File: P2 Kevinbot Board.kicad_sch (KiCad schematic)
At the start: 40 parts, among them J1 Screw_Terminal_01x02, J10 Conn_01x04, J11 Conn_01x04_Male, J12 Conn_02x06_Odd_Even, J13 Conn_01x04, J14 Conn_01x02, J15 Conn_01x04, J16 Conn_02x06_Odd_Even, J2 Conn_01x03_Male, J3 Screw_Terminal_01x02, J30 Conn_01x02_Pin, J31 Conn_01x02, J4 Screw_Terminal_01x02, J5 Screw_Terminal_01x02, J6 Conn_02x06_Odd_Even, J7 Conn_01x04, J8 Conn_02x06_Odd_Even, J9 Screw_Terminal_01x02, Q1 IRLML6402, SW1 SW_Push, U1 P2_EDGE_MODULE_SOCKET, U2 DS18B20

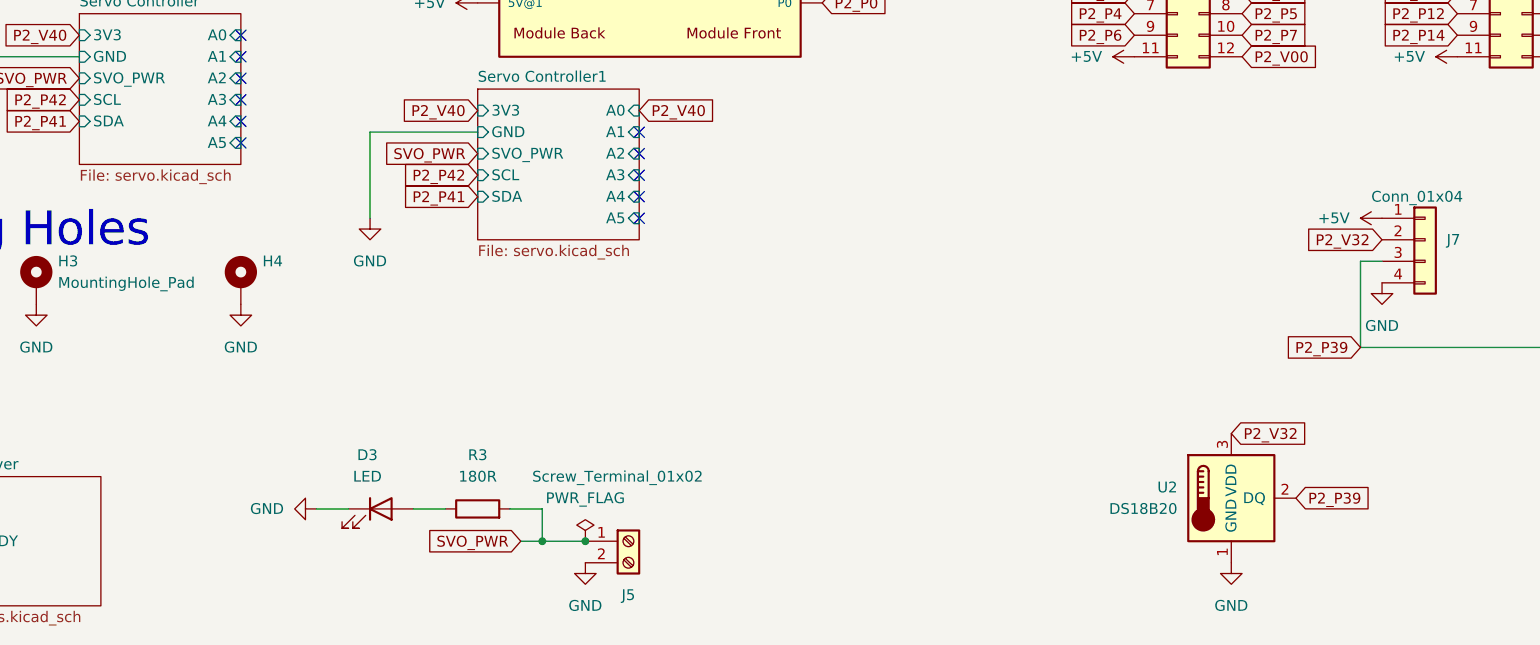
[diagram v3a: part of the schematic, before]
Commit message: Add servo fuse, increase trace width
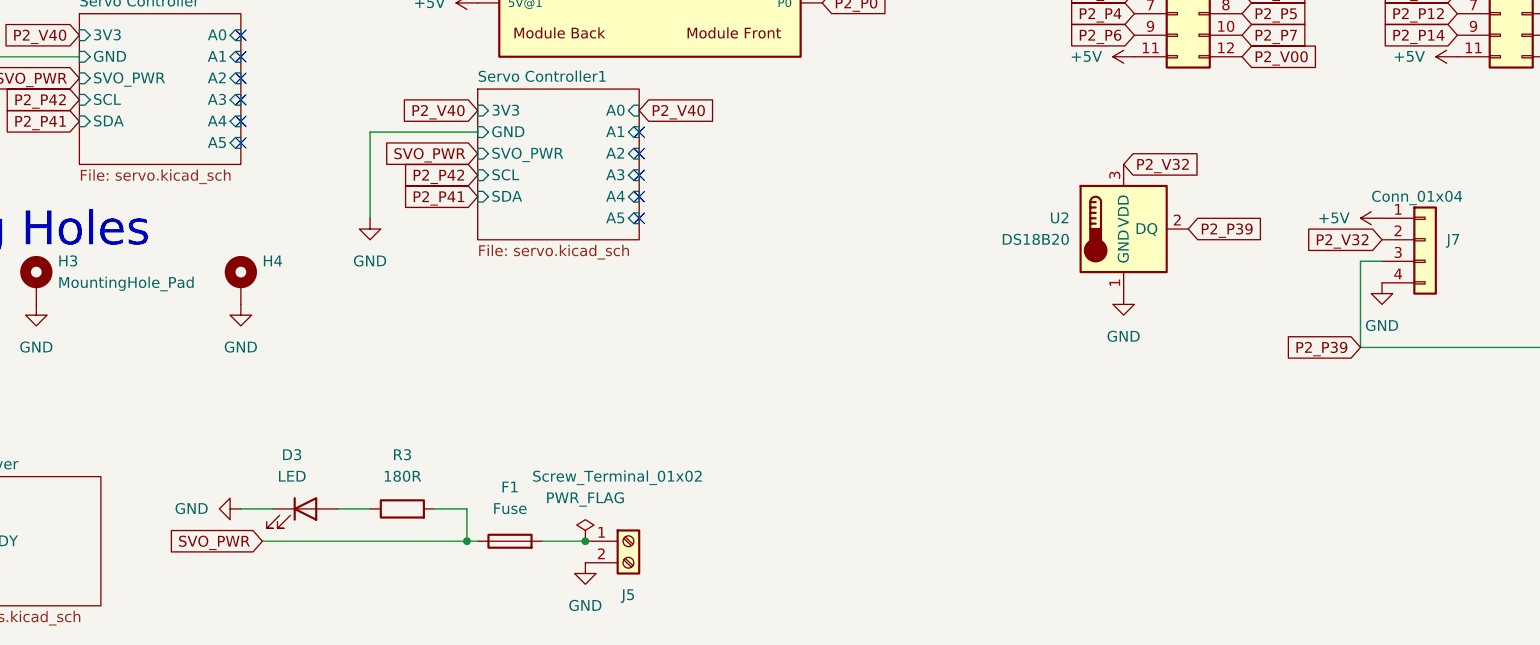
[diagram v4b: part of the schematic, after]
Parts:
- added F1: Fuse, symbol Device:Fuse
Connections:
- net SVO_PWR: now also F1.1; no longer J5.1 (Pin_1)
- new net: F1.2, J5.1 (Pin_1)
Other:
- moved on the sheet: D3, R3, U2
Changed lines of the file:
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@@
 	)
 	(junction
-		(at 133.35 189.23)
+		(at 284.48 69.85)
 		(diameter 0)
 		(color 0 0 0 0)
 	)
 	(junction
-		(at 284.48 69.85)
+		(at 304.8 166.37)
 		(diameter 0)
 		(color 0 0 0 0)
 	)
 	(junction
-		(at 304.8 166.37)
+		(at 198.12 87.63)
 		(diameter 0)
 		(color 0 0 0 0)
 	)
 	(junction
-		(at 138.43 189.23)
+		(at 39.37 33.02)
 		(diameter 0)
 		(color 0 0 0 0)
 	)
 	(junction
-		(at 198.12 87.63)
+		(at 138.43 189.23)
 		(diameter 0)
 		(color 0 0 0 0)
 	)
 	(junction
-		(at 39.37 33.02)
+		(at 273.05 69.85)
 		(diameter 0)
 		(color 0 0 0 0)
 	)
 	(junction
-		(at 273.05 69.85)
+		(at 124.46 189.23)
 		(diameter 0)
 		(color 0 0 0 0)
@@
 	(wire
 		(pts
-			(xy 118.11 185.42) (xy 121.92 185.42)
+			(xy 133.35 189.23) (xy 138.43 189.23)
 		)
 		(stroke
@@
 	(wire
 		(pts
-			(xy 303.53 74.93) (xy 300.99 74.93)
+			(xy 109.22 185.42) (xy 113.03 185.42)
 		)
 		(stroke
@@
 	(wire
 		(pts
-			(xy 133.35 189.23) (xy 138.43 189.23)
+			(xy 303.53 74.93) (xy 300.99 74.93)
 		)
 		(stroke
@@
 	(wire
 		(pts
-			(xy 130.81 189.23) (xy 133.35 189.23)
+			(xy 100.33 189.23) (xy 124.46 189.23)
 		)
 		(stroke
@@
 	(wire
 		(pts
+			(xy 124.46 189.23) (xy 125.73 189.23)
+		)
+		(stroke
+			(width 0)
+			(type default)
+		)
+	)
+	(wire
+		(pts
 			(xy 322.58 86.36) (xy 322.58 85.09)
 		)
@@
 	(wire
 		(pts
-			(xy 133.35 185.42) (xy 133.35 189.23)
+			(xy 124.46 185.42) (xy 124.46 189.23)
 		)
 		(stroke
@@
 	(wire
 		(pts
-			(xy 110.49 185.42) (xy 106.68 185.42)
+			(xy 101.6 185.42) (xy 97.79 185.42)
 		)
 		(stroke
@@
 	(wire
 		(pts
-			(xy 129.54 185.42) (xy 133.35 185.42)
+			(xy 120.65 185.42) (xy 124.46 185.42)
 		)
 		(stroke
@@
 	(global_label "SVO_PWR"
 		(shape input)
-		(at 130.81 189.23 180)
+		(at 100.33 189.23 180)
 		(fields_autoplaced yes)
 		(effects
@@
 		)
 		(property "Intersheetrefs" "${INTERSHEET_REFS}"
-			(at 119.8093 189.1506 0)
+			(at 89.3293 189.1506 0)
 			(effects
 				(font
@@
 	(global_label "P2_P39"
 		(shape input)
-		(at 222.25 184.15 0)
+		(at 209.55 152.4 0)
 		(fields_autoplaced yes)
 		(effects
@@
 		)
 		(property "Intersheetrefs" "${INTERSHEET_REFS}"
-			(at 232.2919 184.15 0)
+			(at 219.5919 152.4 0)
 			(effects
 				(font
@@
 	(global_label "P2_V32"
 		(shape input)
-		(at 214.63 176.53 0)
+		(at 201.93 144.78 0)
 		(fields_autoplaced yes)
 		(effects
@@
 		)
 		(property "Intersheetrefs" "${INTERSHEET_REFS}"
-			(at 224.4905 176.53 0)
+			(at 211.7905 144.78 0)
 			(effects
 				(font
@@
 	(symbol
 		(lib_id "Sensor_Temperature:DS18B20")
-		(at 214.63 184.15 0)
+		(at 201.93 152.4 0)
 		(unit 1)
 		(exclude_from_sim no)
@@
 		(fields_autoplaced yes)
 		(property "Reference" "U2"
-			(at 208.28 182.8799 0)
+			(at 195.58 151.1299 0)
 			(effects
 				(font
@@
 		)
 		(property "Value" "DS18B20"
-			(at 208.28 185.4199 0)
+			(at 195.58 153.6699 0)
 			(effects
 				(font
@@
 		)
 		(property "Footprint" "Package_TO_SOT_THT:TO-92_Inline_Wide"
-			(at 189.23 190.5 0)
+			(at 176.53 158.75 0)
 			(effects
 				(font
@@
 		)
 		(property "Datasheet" "http://datasheets.maximintegrated.com/en/ds/DS18B20.pdf"
-			(at 210.82 177.8 0)
+			(at 198.12 146.05 0)
 			(effects
 				(font
@@
 		)
 		(property "Description" ""
-			(at 214.63 184.15 0)
+			(at 201.93 152.4 0)
 			(effects
 				(font
@@
 	(symbol
 		(lib_id "Device:LED")
-		(at 114.3 185.42 0)
+		(at 105.41 185.42 0)
 		(unit 1)
 		(exclude_from_sim no)
@@
 		(dnp no)
 		(property "Reference" "D3"
-			(at 112.7125 179.07 0)
+			(at 103.8225 179.07 0)
 			(effects
 				(font
@@
 		)
 		(property "Value" "LED"
-			(at 112.7125 181.61 0)
+			(at 103.8225 181.61 0)
 			(effects
 				(font
@@
 		)
 		(property "Footprint" "LED_SMD:LED_0805_2012Metric"
-			(at 114.3 185.42 0)
+			(at 105.41 185.42 0)
 			(effects
 				(font
@@
 		)
 		(property "Datasheet" "https://dammedia.osram.info/media/resource/hires/osram-dam-14795755/LG%20R971_EN.pdf"
-			(at 114.3 185.42 0)
+			(at 105.41 185.42 0)
 			(effects
 				(font
@@
 		)
 		(property "Description" "3.3v (V24) indicator"
-			(at 114.3 185.42 0)
+			(at 105.41 185.42 0)
 			(effects
 				(font
@@
 		)
 		(property "Color" "RED"
-			(at 114.3 185.42 0)
+			(at 105.41 185.42 0)
 			(effects
 				(font
@@
 	(symbol
 		(lib_id "power:GND")
-		(at 214.63 191.77 0)
+		(at 201.93 160.02 0)
 		(unit 1)
 		(exclude_from_sim no)
@@
 		(fields_autoplaced yes)
 		(property "Reference" "#PWR032"
-			(at 214.63 198.12 0)
+			(at 201.93 166.37 0)
 			(effects
 				(font
@@
 		)
 		(property "Value" "GND"
-			(at 214.63 196.85 0)
+			(at 201.93 165.1 0)
 			(effects
 				(font
@@
 		)
 		(property "Footprint" ""
-			(at 214.63 191.77 0)
+			(at 201.93 160.02 0)
 			(effects
 				(font
@@
 		)
 		(property "Datasheet" ""
-			(at 214.63 191.77 0)
+			(at 201.93 160.02 0)
 			(effects
 				(font
@@
 		)
 		(property "Description" ""
-			(at 214.63 191.77 0)
+			(at 201.93 160.02 0)
 			(effects
 				(font
@@
 	(symbol
 		(lib_id "Device:R")
-		(at 125.73 185.42 90)
+		(at 116.84 185.42 90)
 		(unit 1)
 		(exclude_from_sim no)
@@
 		(fields_autoplaced yes)
 		(property "Reference" "R3"
-			(at 125.73 179.07 90)
+			(at 116.84 179.07 90)
 			(effects
 				(font
@@
 		)
 		(property "Value" "180R"
-			(at 125.73 181.61 90)
+			(at 116.84 181.61 90)
 			(effects
 				(font
@@
 		)
 		(property "Footprint" "Resistor_SMD:R_0805_2012Metric"
-			(at 125.73 187.198 90)
+			(at 116.84 187.198 90)
 			(effects
 				(font
@@
 		)
 		(property "Datasheet" "~"
-			(at 125.73 185.42 0)
+			(at 116.84 185.42 0)
 			(effects
 				(font
@@
 		)
 		(property "Description" ""
-			(at 125.73 185.42 0)
+			(at 116.84 185.42 0)
 			(effects
 				(font
@@
 	)
 	(symbol
+		(lib_id "Device:Fuse")
+		(at 129.54 189.23 90)
+		(unit 1)
+		(exclude_from_sim no)
+		(in_bom yes)
+		(on_board yes)
+		(dnp no)
+		(fields_autoplaced yes)
+		(property "Reference" "F1"
+			(at 129.54 182.88 90)
+			(effects
+				(font
+					(size 1.27 1.27)
+				)
+			)
+		)
+		(property "Value" "Fuse"
+			(at 129.54 185.42 90)
+			(effects
+				(font
+					(size 1.27 1.27)
+				)
+			)
+		)
+		(property "Footprint" ""
+			(at 129.54 191.008 90)
+			(effects
+				(font
+					(size 1.27 1.27)
+				)
+				(hide yes)
+			)
+		)
+		(property "Datasheet" "~"
+			(at 129.54 189.23 0)
+			(effects
+				(font
+					(size 1.27 1.27)
+				)
+				(hide yes)
+			)
+		)
+		(property "Description" "Fuse"
+			(at 129.54 189.23 0)
+			(effects
+				(font
+					(size 1.27 1.27)
+				)
+				(hide yes)
+			)
+		)
+		(pin "2"
+		)
+		(pin "1"
+		)
+		(instances
+			(project ""
+				(path "/362ca48c-0b77-4943-b8b3-fc15ab97f30d"
+					(reference "F1")
+					(unit 1)
+				)
+			)
+		)
+	)
+	(symbol
 		(lib_id "power:+5V")
 		(at 81.28 31.75 0)
@@
 	(symbol
 		(lib_id "power:GND")
-		(at 106.68 185.42 270)
+		(at 97.79 185.42 270)
 		(unit 1)
 		(exclude_from_sim no)
@@
 		(fields_autoplaced yes)
 		(property "Reference" "#PWR019"
-			(at 100.33 185.42 0)
+			(at 91.44 185.42 0)
 			(effects
 				(font
@@
 		)
 		(property "Value" "GND"
-			(at 102.87 185.4199 90)
+			(at 93.98 185.4199 90)
 			(effects
 				(font
@@
 		)
 		(property "Footprint" ""
-			(at 106.68 185.42 0)
+			(at 97.79 185.42 0)
 			(effects
 				(font
@@
 		)
 		(property "Datasheet" ""
-			(at 106.68 185.42 0)
+			(at 97.79 185.42 0)
 			(effects
 				(font
@@
 		)
 		(property "Description" ""
-			(at 106.68 185.42 0)
+			(at 97.79 185.42 0)
 			(effects
 				(font

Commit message: Add new kevinbot logo
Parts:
- F1: footprint (none) -> Fuse:Fuseholder_Blade_Mini_Keystone_3568
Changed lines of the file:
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@@
 			)
 		)
-		(property "Footprint" ""
+		(property "Footprint" "Fuse:Fuseholder_Blade_Mini_Keystone_3568"
 			(at 129.54 191.008 90)
 			(effects

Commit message: Change logo, led resistors
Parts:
- D1, D2, D3: Part Number (none) -> LS R976-NR-1-0-20-R18
- R1: value 360R -> 620R
- R2: value 180R -> 270R
- R3: value 180R -> 820R
- R8: footprint Resistor_THT:R_Axial_DIN0207_L6.3mm_D2.5mm_P10.16mm_Horizontal -> Resistor_SMD:R_0603_1608Metric
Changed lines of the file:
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@@
 			)
 		)
-		(property "Value" "180R"
+		(property "Value" "270R"
 			(at 88.9 50.8 90)
 			(effects
@@
 			)
 		)
-		(property "Datasheet" "https://dammedia.osram.info/media/resource/hires/osram-dam-14795755/LG%20R971_EN.pdf"
+		(property "Datasheet" "https://dammedia.osram.info/media/resource/hires/osram-dam-5178068/LS%20R976_EN.pdf"
 			(at 77.47 54.61 0)
 			(effects
@@
 			)
 		)
+		(property "Part Number" "LS R976-NR-1-0-20-R18"
+			(at 77.47 54.61 0)
+			(effects
+				(font
+					(size 1.27 1.27)
+				)
+				(hide yes)
+			)
+		)
 		(pin "1"
 		)
@@
 			)
 		)
-		(property "Datasheet" "https://dammedia.osram.info/media/resource/hires/osram-dam-14795755/LG%20R971_EN.pdf"
+		(property "Datasheet" "https://dammedia.osram.info/media/resource/hires/osram-dam-5178068/LS%20R976_EN.pdf"
 			(at 105.41 185.42 0)
 			(effects
@@
 			)
 		)
+		(property "Part Number" "LS R976-NR-1-0-20-R18"
+			(at 105.41 185.42 0)
+			(show_name yes)
+			(effects
+				(font
+					(size 1.27 1.27)
+				)
+				(hide yes)
+			)
+		)
 		(pin "1"
 		)
@@
 		(fields_autoplaced yes)
 		(property "Reference" "R8"
-			(at 321.31 161.29 90)
+			(at 321.31 160.02 90)
 			(effects
 				(font
@@
 		)
 		(property "Value" "4K7"
-			(at 321.31 163.83 90)
+			(at 321.31 162.56 90)
 			(effects
 				(font
@@
 			)
 		)
-		(property "Footprint" "Resistor_THT:R_Axial_DIN0207_L6.3mm_D2.5mm_P10.16mm_Horizontal"
+		(property "Footprint" "Resistor_SMD:R_0603_1608Metric"
 			(at 321.31 168.148 90)
 			(effects
@@
 			)
 		)
-		(property "Value" "360R"
+		(property "Value" "620R"
 			(at 45.72 50.8 90)
 			(effects
@@
 			)
 		)
-		(property "Value" "180R"
+		(property "Value" "820R"
 			(at 116.84 181.61 90)
 			(effects
@@
 			)
 		)
-		(property "Datasheet" "https://dammedia.osram.info/media/resource/hires/osram-dam-14795755/LG%20R971_EN.pdf"
+		(property "Datasheet" "https://dammedia.osram.info/media/resource/hires/osram-dam-5178068/LS%20R976_EN.pdf"
 			(at 34.29 54.61 0)
 			(effects
@@
 			(effects
 				(font
+					(size 1.27 1.27)
+				)
+				(hide yes)
+			)
+		)
+		(property "Part Number" "LS R976-NR-1-0-20-R18"
+			(at 34.29 54.61 0)
+			(effects
+				(font

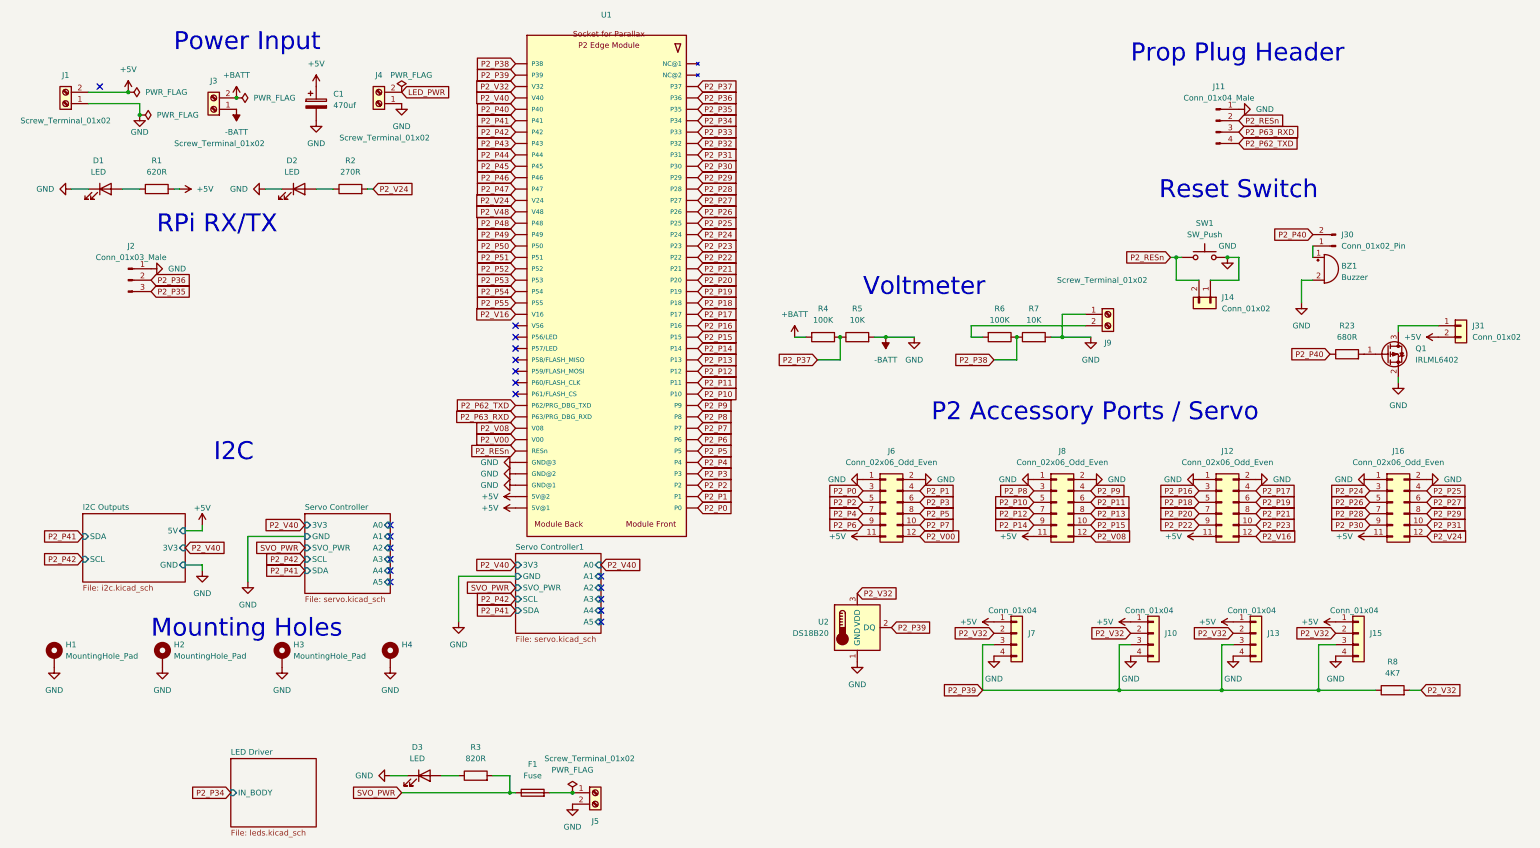
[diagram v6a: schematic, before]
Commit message: DRC fixes, add missing library, misc
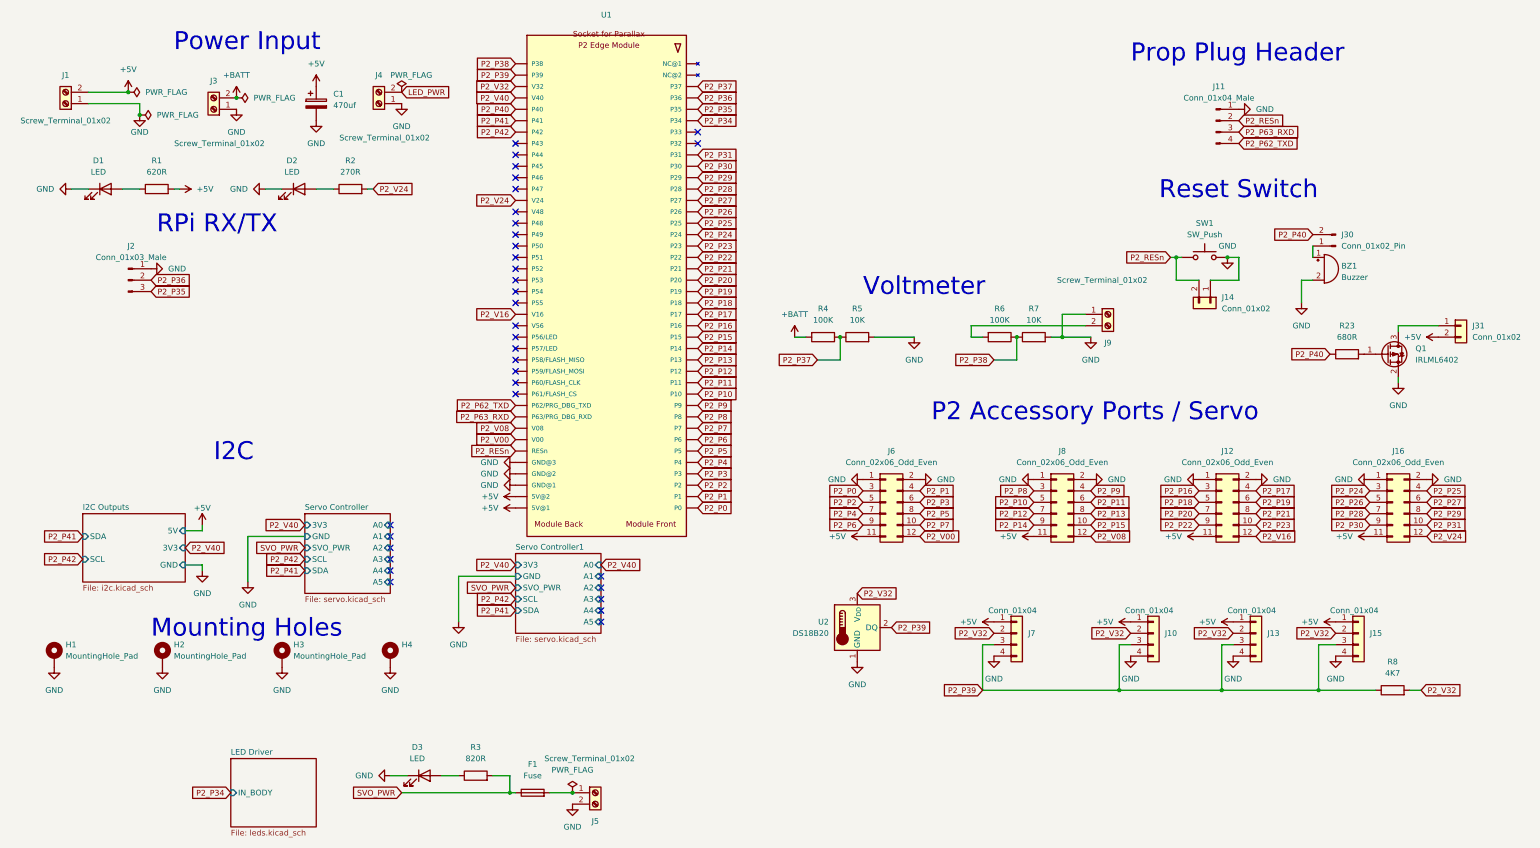
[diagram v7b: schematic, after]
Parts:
- J11: symbol Connector:Conn_01x04_Male -> Connector:Conn_01x04_Pin
- J2: symbol Connector:Conn_01x03_Male -> Connector:Conn_01x03_Pin
- R1: Part Number (none) -> RC0805FR-07620RL
- R2: Part Number (none) -> RC0805FR-07270RL
- R3: Part Number (none) -> RC0805FR-07820RL
- R4, R6: Part Number (none) -> YR1B100KCC
- R5, R7: Part Number (none) -> YR1B10KCC
- R8: Part Number (none) -> RC0603FR-074K7L
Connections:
- net -BATT renamed GND
- net P2_P32: no longer names the net of U1.8 (P32)
- net P2_P33: no longer names the net of U1.7 (P33)
- net P2_P43: no longer names the net of U1.73 (P43)
- net P2_P44: no longer names the net of U1.72 (P44)
- net P2_P45: no longer names the net of U1.71 (P45)
- net P2_P46: no longer names the net of U1.70 (P46)
- net P2_P47: no longer names the net of U1.69 (P47)
- net P2_P48: no longer names the net of U1.66 (P48)
- net P2_P49: no longer names the net of U1.65 (P49)
- net P2_P50: no longer names the net of U1.64 (P50)
- net P2_P51: no longer names the net of U1.63 (P51)
- net P2_P52: no longer names the net of U1.62 (P52)
- net P2_P53: no longer names the net of U1.61 (P53)
- net P2_P54: no longer names the net of U1.60 (P54)
- net P2_P55: no longer names the net of U1.59 (P55)
- net P2_V48: no longer names the net of U1.67 (V48)
- no-connect marks 19 -> 34
